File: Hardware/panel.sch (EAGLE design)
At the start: 100 parts, among them Q1 BC817-40LT1SMD, Q10 BC807-16LT1SMD, Q11 BC807-16LT1SMD, Q12 BC807-16LT1SMD, Q13 BC817-40LT1SMD, Q14 BC817-40LT1SMD, Q15 BC817-40LT1SMD, Q16 BC817-40LT1SMD, Q17 BC817-40LT1SMD, Q18 BC817-40LT1SMD, Q19 BC817-40LT1SMD, Q2 BC817-40LT1SMD, Q3 BC817-40LT1SMD, Q4 BC817-40LT1SMD, Q5 BC817-40LT1SMD, Q6 BC807-16LT1SMD, Q7 BC807-16LT1SMD, Q8 BC807-16LT1SMD, Q9 BC807-16LT1SMD, U1 MC7805CDT, X1 B16B-PHDSS, X2 52746-20

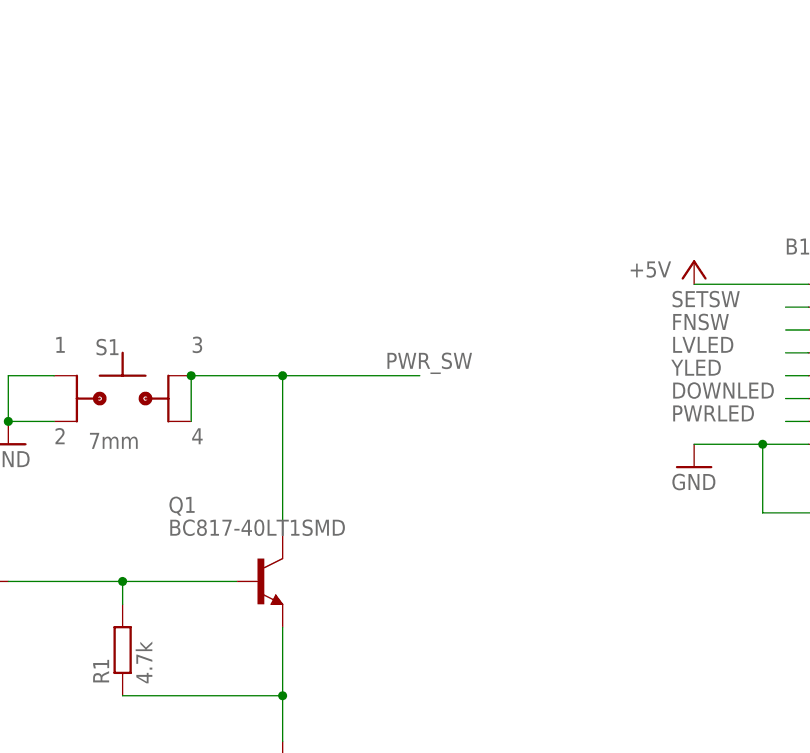
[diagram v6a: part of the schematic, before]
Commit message: добавил RC-цепочку для устранения дребезга
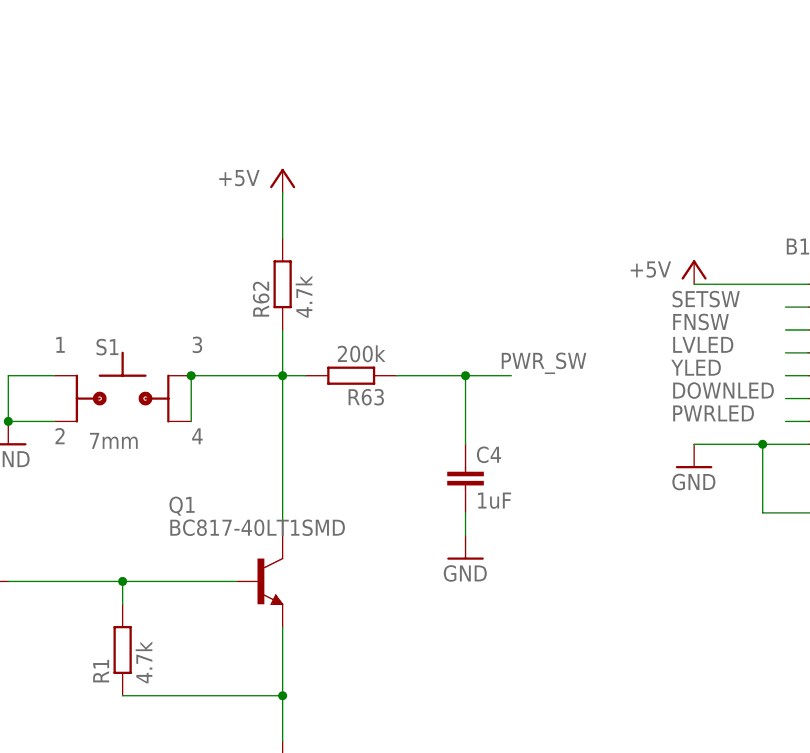
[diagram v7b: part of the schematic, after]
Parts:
- added C4: 1uF, rcl:C-EUC0805
- added R62: 4.7k, rcl:R-EU_R0805
- added R63: 200k, rcl:R-EU_R0805
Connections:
- new net N$49: Q1.C, R62.1, R63.2, S1.1@A, S1.1@B
- net +5V: now also R62.2
- net GND: now also C4.2
- net PWR_SW: now also C4.1, R63.1; no longer Q1.C, S1.1@A, S1.1@B
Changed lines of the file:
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@@
 <part name="R48" library="rcl" library_urn="urn:adsk.eagle:library:334" deviceset="R-EU_" device="R2512" package3d_urn="urn:adsk.eagle:package:23545/2" value="150"/>
 <part name="R49" library="rcl" library_urn="urn:adsk.eagle:library:334" deviceset="R-EU_" device="R2512" package3d_urn="urn:adsk.eagle:package:23545/2" value="150"/>
+<part name="R62" library="rcl" library_urn="urn:adsk.eagle:library:334" deviceset="R-EU_" device="R0805" package3d_urn="urn:adsk.eagle:package:23553/2" value="4.7k"/>
+<part name="R63" library="rcl" library_urn="urn:adsk.eagle:library:334" deviceset="R-EU_" device="R0805" package3d_urn="urn:adsk.eagle:package:23553/2" value="200k"/>
+<part name="C4" library="rcl" library_urn="urn:adsk.eagle:library:334" deviceset="C-EU" device="C0805" package3d_urn="urn:adsk.eagle:package:23617/2" value="1uF"/>
+<part name="P+18" library="supply1" library_urn="urn:adsk.eagle:library:371" deviceset="+5V" device=""/>
+<part name="GND23" library="supply1" library_urn="urn:adsk.eagle:library:371" deviceset="GND" device=""/>
 </parts>
 <sheets>
@@
 <attribute name="VALUE" x="214.63" y="174.498" size="1.778" layer="96"/>
 </instance>
+<instance part="R62" gate="G$1" x="-10.16" y="66.04" smashed="yes" rot="R90">
+<attribute name="NAME" x="-11.6586" y="62.23" size="1.778" layer="95" rot="R90"/>
+<attribute name="VALUE" x="-6.858" y="62.23" size="1.778" layer="96" rot="R90"/>
+</instance>
+<instance part="R63" gate="G$1" x="-2.54" y="55.88" smashed="yes" rot="R180">
+<attribute name="NAME" x="1.27" y="54.3814" size="1.778" layer="95" rot="R180"/>
+<attribute name="VALUE" x="1.27" y="59.182" size="1.778" layer="96" rot="R180"/>
+</instance>
+<instance part="C4" gate="G$1" x="10.16" y="45.72" smashed="yes">
+<attribute name="NAME" x="11.303" y="46.2026" size="1.778" layer="95"/>
+<attribute name="VALUE" x="11.303" y="41.1226" size="1.778" layer="96"/>
+</instance>
+<instance part="P+18" gate="1" x="-10.16" y="78.74" smashed="yes">
+<attribute name="VALUE" x="-12.7" y="78.74" size="1.778" layer="96" rot="R180"/>
+</instance>
+<instance part="GND23" gate="1" x="10.16" y="35.56" smashed="yes">
+<attribute name="VALUE" x="7.62" y="33.02" size="1.778" layer="96"/>
+</instance>
 </instances>
 <busses>
@@
 <net name="PWR_SW" class="2">
 <segment>
-<pinref part="S1" gate="G$1" pin="1@A"/>
-<wire x1="-20.32" y1="55.88" x2="-10.16" y2="55.88" width="0.1524" layer="91"/>
-<label x="1.27" y="56.642" size="1.778" layer="95"/>
-<pinref part="S1" gate="G$1" pin="1@B"/>
-<wire x1="-10.16" y1="55.88" x2="5.08" y2="55.88" width="0.1524" layer="91"/>
-<wire x1="-20.32" y1="50.8" x2="-20.32" y2="55.88" width="0.1524" layer="91"/>
-<junction x="-20.32" y="55.88"/>
-<wire x1="-10.16" y1="55.88" x2="-10.16" y2="38.1" width="0.1524" layer="91"/>
-<junction x="-10.16" y="55.88"/>
-<pinref part="Q1" gate="G$1" pin="C"/>
-</segment>
-<segment>
 <pinref part="X1" gate="G$1" pin="2"/>
 <wire x1="66.04" y1="66.04" x2="63.5" y2="66.04" width="0.1524" layer="91"/>
 <label x="73.914" y="66.802" size="1.778" layer="95"/>
+</segment>
+<segment>
+<wire x1="2.54" y1="55.88" x2="10.16" y2="55.88" width="0.1524" layer="91"/>
+<label x="13.97" y="56.642" size="1.778" layer="95"/>
+<pinref part="R63" gate="G$1" pin="1"/>
+<pinref part="C4" gate="G$1" pin="1"/>
+<wire x1="10.16" y1="55.88" x2="15.24" y2="55.88" width="0.1524" layer="91"/>
+<wire x1="10.16" y1="48.26" x2="10.16" y2="55.88" width="0.1524" layer="91"/>
+<junction x="10.16" y="55.88"/>
 </segment>
 </net>
@@
 <pinref part="P+17" gate="1" pin="+5V"/>
 <wire x1="-129.54" y1="-48.26" x2="-129.54" y2="-50.8" width="0.1524" layer="91"/>
+</segment>
+<segment>
+<pinref part="R62" gate="G$1" pin="2"/>
+<pinref part="P+18" gate="1" pin="+5V"/>
+<wire x1="-10.16" y1="71.12" x2="-10.16" y2="76.2" width="0.1524" layer="91"/>
 </segment>
 </net>
@@
 <pinref part="GND22" gate="1" pin="GND"/>
 <junction x="182.88" y="50.8"/>
+</segment>
+<segment>
+<pinref part="C4" gate="G$1" pin="2"/>
+<pinref part="GND23" gate="1" pin="GND"/>
+<wire x1="10.16" y1="40.64" x2="10.16" y2="38.1" width="0.1524" layer="91"/>
 </segment>
 </net>
@@
 </segment>
 </net>
+<net name="N$49" class="2">
+<segment>
+<pinref part="S1" gate="G$1" pin="1@A"/>
+<wire x1="-20.32" y1="55.88" x2="-10.16" y2="55.88" width="0.1524" layer="91"/>
+<pinref part="S1" gate="G$1" pin="1@B"/>
+<wire x1="-20.32" y1="50.8" x2="-20.32" y2="55.88" width="0.1524" layer="91"/>
+<junction x="-20.32" y="55.88"/>
+<wire x1="-10.16" y1="55.88" x2="-10.16" y2="38.1" width="0.1524" layer="91"/>
+<junction x="-10.16" y="55.88"/>
+<pinref part="Q1" gate="G$1" pin="C"/>
+<wire x1="-10.16" y1="55.88" x2="-7.62" y2="55.88" width="0.1524" layer="91"/>
+<pinref part="R63" gate="G$1" pin="2"/>
+<pinref part="R62" gate="G$1" pin="1"/>
+<wire x1="-10.16" y1="55.88" x2="-10.16" y2="60.96" width="0.1524" layer="91"/>
+</segment>
+</net>

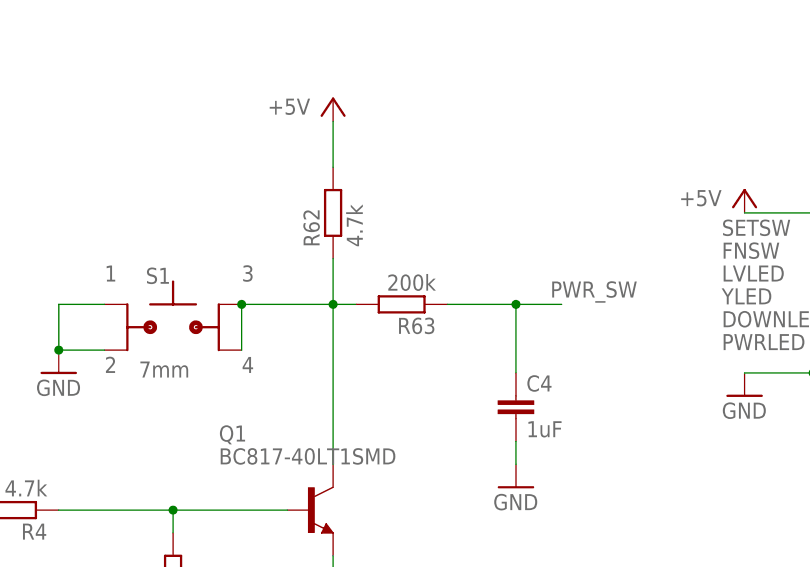
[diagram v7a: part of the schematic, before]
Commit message: экспеиментально подобрал параметры цепочки кнопки питания, чтобы она срабатывала без проблем
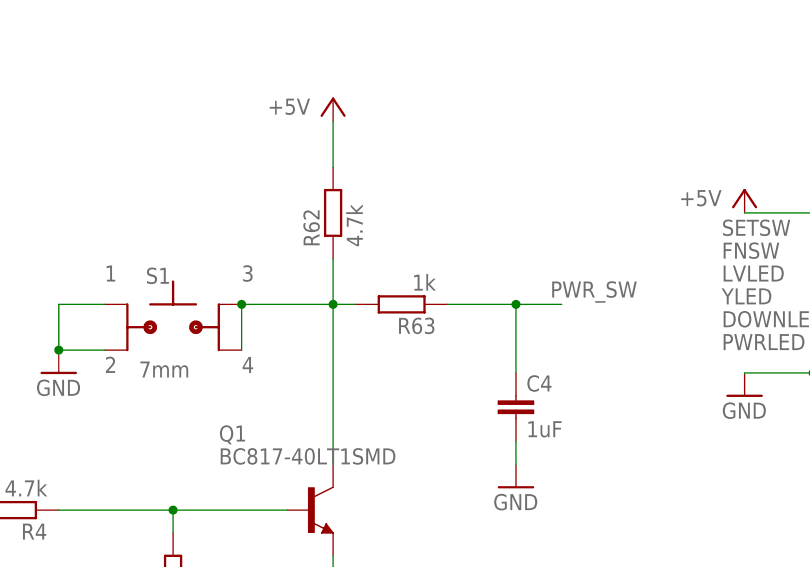
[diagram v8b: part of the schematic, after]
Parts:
- R63: value 200k -> 1k
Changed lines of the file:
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@@
 <part name="R49" library="rcl" library_urn="urn:adsk.eagle:library:334" deviceset="R-EU_" device="R2512" package3d_urn="urn:adsk.eagle:package:23545/2" value="150"/>
 <part name="R62" library="rcl" library_urn="urn:adsk.eagle:library:334" deviceset="R-EU_" device="R0805" package3d_urn="urn:adsk.eagle:package:23553/2" value="4.7k"/>
-<part name="R63" library="rcl" library_urn="urn:adsk.eagle:library:334" deviceset="R-EU_" device="R0805" package3d_urn="urn:adsk.eagle:package:23553/2" value="200k"/>
+<part name="R63" library="rcl" library_urn="urn:adsk.eagle:library:334" deviceset="R-EU_" device="R0805" package3d_urn="urn:adsk.eagle:package:23553/2" value="1k"/>
 <part name="C4" library="rcl" library_urn="urn:adsk.eagle:library:334" deviceset="C-EU" device="C0805" package3d_urn="urn:adsk.eagle:package:23617/2" value="1uF"/>
 <part name="P+18" library="supply1" library_urn="urn:adsk.eagle:library:371" deviceset="+5V" device=""/>
